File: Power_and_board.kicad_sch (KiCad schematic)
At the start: 22 parts, among them J7 PWR_HEADER, U1 AMS1117-3.3

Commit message: v2.1 export, renders
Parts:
- J7: now left out of the parts list
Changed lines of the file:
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@@
   (title_block
     (title "Spotify Neopixel Visualizer")
-    (date "2023-10-08")
-    (rev "v2.0.9")
+    (date "2023-10-15")
+    (rev "v2.1")
     (comment 2 "the Spotify API to react to the currently playing song on Spotify.")
     (comment 3 "A modular, internet connected LED strip driver that uses ")
@@
   (junction (at 153.035 100.33) (diameter 0) (color 0 0 0 0)
   )
-  (junction (at 137.16 107.95) (diameter 0) (color 0 0 0 0)
-  )
   (junction (at 97.79 100.33) (diameter 0) (color 0 0 0 0)
   )
@@
     (stroke (width 0) (type default))
   )
+  (wire (pts (xy 140.335 109.22) (xy 140.335 107.95))
+    (stroke (width 0) (type default))
+  )
   (wire (pts (xy 140.335 100.33) (xy 147.32 100.33))
     (stroke (width 0) (type default))
@@
     (stroke (width 0) (type default))
   )
-  (wire (pts (xy 137.16 107.95) (xy 140.335 107.95))
-    (stroke (width 0) (type default))
-  )
   (wire (pts (xy 140.335 86.36) (xy 138.43 86.36))
     (stroke (width 0) (type default))
@@
     (stroke (width 0) (type default))
   )
+  (wire (pts (xy 132.715 107.95) (xy 140.335 107.95))
+    (stroke (width 0) (type default))
+  )
   (wire (pts (xy 155.575 165.735) (xy 161.925 165.735))
     (stroke (width 0) (type default))
@@
     (stroke (width 0) (type default))
   )
-  (wire (pts (xy 132.715 107.95) (xy 137.16 107.95))
-    (stroke (width 0) (type default))
-  )
   (wire (pts (xy 166.37 91.44) (xy 160.02 91.44))
     (stroke (width 0) (type default))
@@
   )
   (text "Allows disconnect of USB's VBUS \nfrom the Board's VCC, to prevent \nfeedback when programming the \nboard while it's plugged in. "
-    (at 113.665 81.915 0)
+    (at 113.665 83.185 0)
     (effects (font (size 1 1)) (justify left bottom))
   )
@@
     (effects (font (size 1.27 1.27)) (justify right))
   )
-  (hierarchical_label "VBUS" (shape input) (at 140.335 70.485 0) (fields_autoplaced)
-    (effects (font (size 1.27 1.27)) (justify left))
+  (hierarchical_label "VBUS" (shape input) (at 140.335 70.485 180) (fields_autoplaced)
+    (effects (font (size 1.27 1.27)) (justify right))
   )
   (hierarchical_label "3.3V" (shape output) (at 201.295 100.33 0) (fields_autoplaced)
@@
     )
   )
-  (symbol (lib_id "power:Earth") (at 137.16 107.95 0) (unit 1)
+  (symbol (lib_id "power:Earth") (at 140.335 109.22 0) (unit 1)
     (in_bom yes) (on_board yes) (dnp no) (fields_autoplaced)
-    (property "Reference" "#PWR05" (at 137.16 114.3 0)
-      (effects (font (size 1.27 1.27)) hide)
-    )
-    (property "Value" "Earth" (at 137.16 111.76 0)
-      (effects (font (size 1.27 1.27)) hide)
-    )
-    (property "Footprint" "" (at 137.16 107.95 0)
-      (effects (font (size 1.27 1.27)) hide)
-    )
-    (property "Datasheet" "~" (at 137.16 107.95 0)
+    (property "Reference" "#PWR05" (at 140.335 115.57 0)
+      (effects (font (size 1.27 1.27)) hide)
+    )
+    (property "Value" "Earth" (at 140.335 113.03 0)
+      (effects (font (size 1.27 1.27)) hide)
+    )
+    (property "Footprint" "" (at 140.335 109.22 0)
+      (effects (font (size 1.27 1.27)) hide)
+    )
+    (property "Datasheet" "~" (at 140.335 109.22 0)
       (effects (font (size 1.27 1.27)) hide)
     )
@@
   )
   (symbol (lib_id "Connector_Generic:Conn_01x02") (at 159.385 116.205 0) (mirror x) (unit 1)
-    (in_bom yes) (on_board yes) (dnp no)
+    (in_bom no) (on_board yes) (dnp no)
     (property "Reference" "J7" (at 162.56 116.205 0)
       (effects (font (size 1.27 1.27)) (justify left))

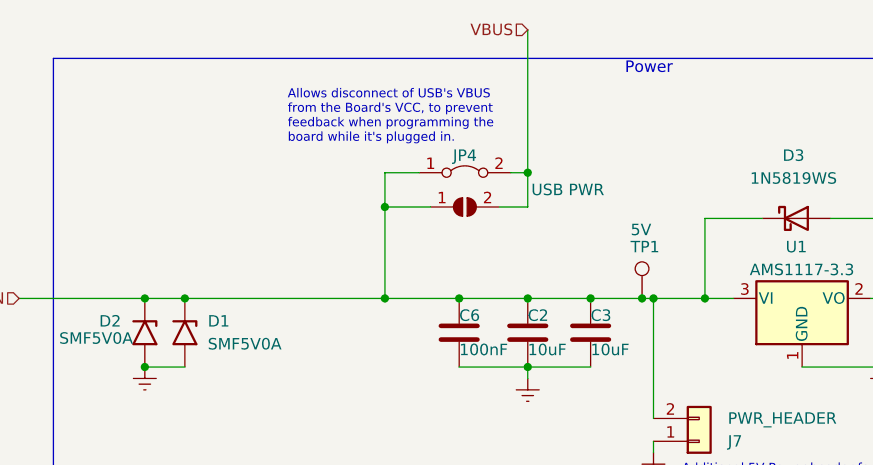
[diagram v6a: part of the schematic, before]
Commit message: added power led disconnect and cleaned up some traces
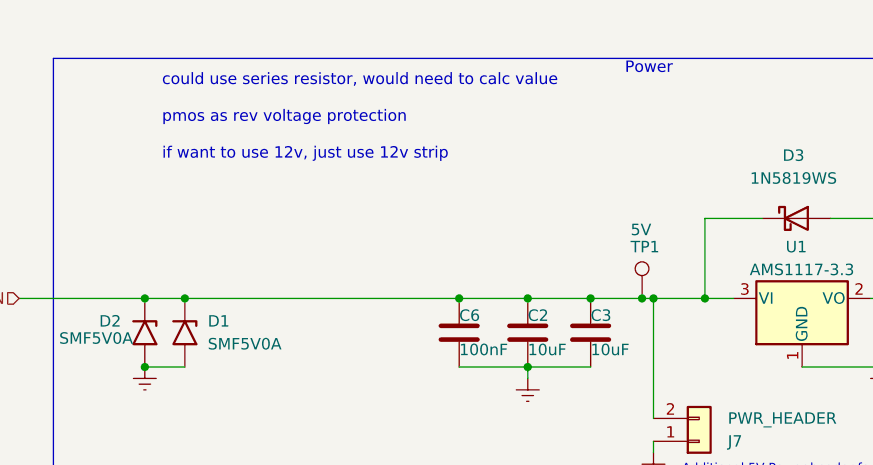
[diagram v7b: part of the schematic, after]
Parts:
- removed JP3: USB PWR, Jumper:SolderJumper-2_P1.3mm_Open_RoundedPad1.0x1.5mm, symbol Jumper:SolderJumper_2_Open
- removed JP4: Jumper_2_Bridged, Connector_PinHeader_2.54mm:PinHeader_1x02_P2.54mm_Vertical, symbol Jumper:Jumper_2_Bridged
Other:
- note added: "could use series resistor, would need to calc value pmos as rev voltage protection if want to use 12v, just use 12v strip"
- note removed: "Allows disconnect of USB's VBUS from the Board's VCC, to prevent feedback when programming the board while it's plugged in."
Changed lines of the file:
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@@
   (junction (at 183.515 100.33) (diameter 0) (color 0 0 0 0)
   )
-  (junction (at 124.46 90.17) (diameter 0) (color 0 0 0 0)
-  )
-  (junction (at 140.335 86.36) (diameter 0) (color 0 0 0 0)
-  )
   (junction (at 153.035 100.33) (diameter 0) (color 0 0 0 0)
   )
@@
   (junction (at 179.705 107.95) (diameter 0) (color 0 0 0 0)
   )
-  (junction (at 124.46 100.33) (diameter 0) (color 0 0 0 0)
-  )
   (junction (at 148.59 165.735) (diameter 0) (color 0 0 0 0)
   )
@@
     (stroke (width 0) (type default))
   )
-  (wire (pts (xy 124.46 100.33) (xy 132.715 100.33))
-    (stroke (width 0) (type default))
-  )
   (wire (pts (xy 148.59 165.735) (xy 148.59 167.64))
     (stroke (width 0) (type default))
@@
     (stroke (width 0) (type default))
   )
-  (wire (pts (xy 140.335 86.36) (xy 138.43 86.36))
-    (stroke (width 0) (type default))
-  )
   (wire (pts (xy 179.705 107.95) (xy 183.515 107.95))
     (stroke (width 0) (type default))
@@
     (stroke (width 0) (type default))
   )
-  (wire (pts (xy 124.46 86.36) (xy 128.27 86.36))
-    (stroke (width 0) (type default))
-  )
   (wire (pts (xy 141.605 165.735) (xy 148.59 165.735))
     (stroke (width 0) (type default))
   )
-  (wire (pts (xy 102.235 100.33) (xy 124.46 100.33))
+  (wire (pts (xy 102.235 100.33) (xy 132.715 100.33))
     (stroke (width 0) (type default))
   )
@@
     (stroke (width 0) (type default))
   )
-  (wire (pts (xy 140.335 86.36) (xy 140.335 90.17))
-    (stroke (width 0) (type default))
-  )
   (wire (pts (xy 147.32 100.33) (xy 153.035 100.33))
     (stroke (width 0) (type default))
@@
     (stroke (width 0) (type default))
   )
-  (wire (pts (xy 124.46 90.17) (xy 124.46 100.33))
-    (stroke (width 0) (type default))
-  )
   (wire (pts (xy 154.305 116.205) (xy 154.305 117.475))
     (stroke (width 0) (type default))
   )
-  (wire (pts (xy 124.46 90.17) (xy 129.54 90.17))
-    (stroke (width 0) (type default))
-  )
-  (wire (pts (xy 137.16 90.17) (xy 140.335 90.17))
-    (stroke (width 0) (type default))
-  )
   (wire (pts (xy 173.99 91.44) (xy 179.705 91.44))
     (stroke (width 0) (type default))
   )
-  (wire (pts (xy 140.335 70.485) (xy 140.335 86.36))
-    (stroke (width 0) (type default))
-  )
   (wire (pts (xy 154.305 100.33) (xy 160.02 100.33))
     (stroke (width 0) (type default))
@@
     (stroke (width 0) (type default))
   )
-  (wire (pts (xy 124.46 86.36) (xy 124.46 90.17))
-    (stroke (width 0) (type default))
-  )
   (wire (pts (xy 160.02 100.33) (xy 163.195 100.33))
     (stroke (width 0) (type default))
@@
     (fill (type none))
   )
-  (text "Allows disconnect of USB's VBUS \nfrom the Board's VCC, to prevent \nfeedback when programming the \nboard while it's plugged in. "
-    (at 113.665 83.185 0)
-    (effects (font (size 1 1)) (justify left bottom))
+  (text "could use series resistor, would need to calc value\n\npmos as rev voltage protection\n\nif want to use 12v, just use 12v strip"
+    (at 99.695 85.09 0)
+    (effects (font (size 1.27 1.27)) (justify left bottom))
   )
   (text "Board" (at 147.32 154.94 0)
@@
     (effects (font (size 1.27 1.27)) (justify right))
   )
-  (hierarchical_label "VBUS" (shape input) (at 140.335 70.485 180) (fields_autoplaced)
-    (effects (font (size 1.27 1.27)) (justify right))
-  )
   (hierarchical_label "3.3V" (shape output) (at 201.295 100.33 0) (fields_autoplaced)
     (effects (font (size 1.27 1.27)) (justify left))
@@
         (path "/745f5767-ebad-4719-b66e-073bc90db4bc"
           (reference "H1") (unit 1)
-        )
-      )
-    )
-  )
-  (symbol (lib_id "Jumper:Jumper_2_Bridged") (at 133.35 86.36 0) (unit 1)
-    (in_bom no) (on_board yes) (dnp no)
-    (property "Reference" "JP4" (at 133.35 84.455 0)
-      (effects (font (size 1.27 1.27)))
-    )
-    (property "Value" "Jumper_2_Bridged" (at 133.35 83.185 0)
-      (effects (font (size 1.27 1.27)) hide)
-    )
-    (property "Footprint" "Connector_PinHeader_2.54mm:PinHeader_1x02_P2.54mm_Vertical" (at 133.35 86.36 0)
-      (effects (font (size 1.27 1.27)) hide)
-    )
-    (property "Datasheet" "~" (at 133.35 86.36 0)
-      (effects (font (size 1.27 1.27)) hide)
-    )
-    (pin "1")
-    (pin "2")
-    (instances
-      (project "iot_led_strip_pcb"
-        (path "/745f5767-ebad-4719-b66e-073bc90db4bc/cfe13250-7fa5-4f24-964e-9463793dd38d"
-          (reference "JP4") (unit 1)
-        )
-        (path "/745f5767-ebad-4719-b66e-073bc90db4bc"
-          (reference "JP1") (unit 1)
         )
       )
@@
         )
       )
-    )
-  )
-  (symbol (lib_id "Jumper:SolderJumper_2_Open") (at 133.35 90.17 0) (unit 1)
-    (in_bom no) (on_board yes) (dnp no)
-    (property "Reference" "JP3" (at 132.08 92.71 0)
-      (effects (font (size 1.27 1.27)) hide)
-    )
-    (property "Value" "USB PWR" (at 144.78 88.265 0)
-      (effects (font (size 1.27 1.27)))
-    )
-    (property "Footprint" "Jumper:SolderJumper-2_P1.3mm_Open_RoundedPad1.0x1.5mm" (at 133.35 90.17 0)
-      (effects (font (size 1.27 1.27)) hide)
-    )
-    (property "Datasheet" "~" (at 133.35 90.17 0)
-      (effects (font (size 1.27 1.27)) hide)
-    )
-    (pin "1")
-    (pin "2")
-    (instances
-      (project "iot_led_strip_pcb"
-        (path "/745f5767-ebad-4719-b66e-073bc90db4bc/cfe13250-7fa5-4f24-964e-9463793dd38d"
-          (reference "JP3") (unit 1)
-        )
-        (path "/745f5767-ebad-4719-b66e-073bc90db4bc"
-          (reference "JP2") (unit 1)
-        )
-      )
